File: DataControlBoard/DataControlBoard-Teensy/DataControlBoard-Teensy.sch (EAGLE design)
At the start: 1 part

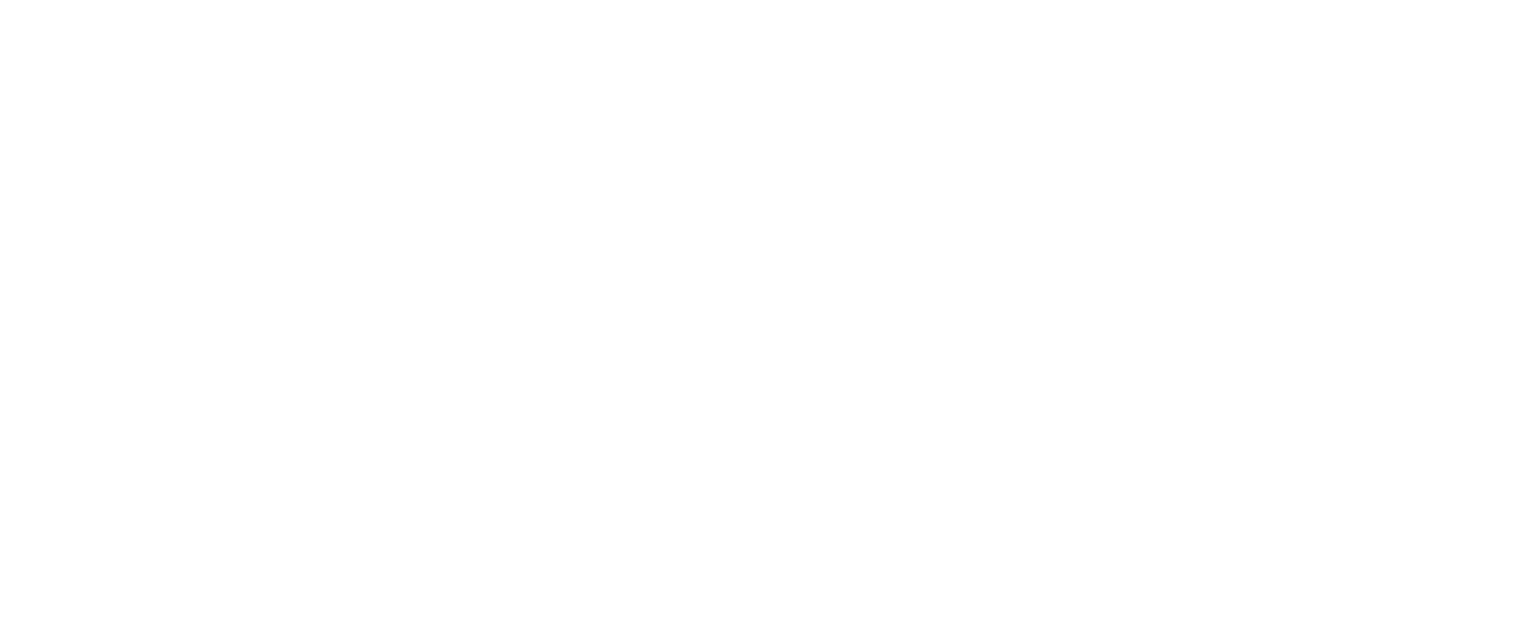
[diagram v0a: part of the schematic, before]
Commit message: Added micro-d25 connectors to lib, added to schem
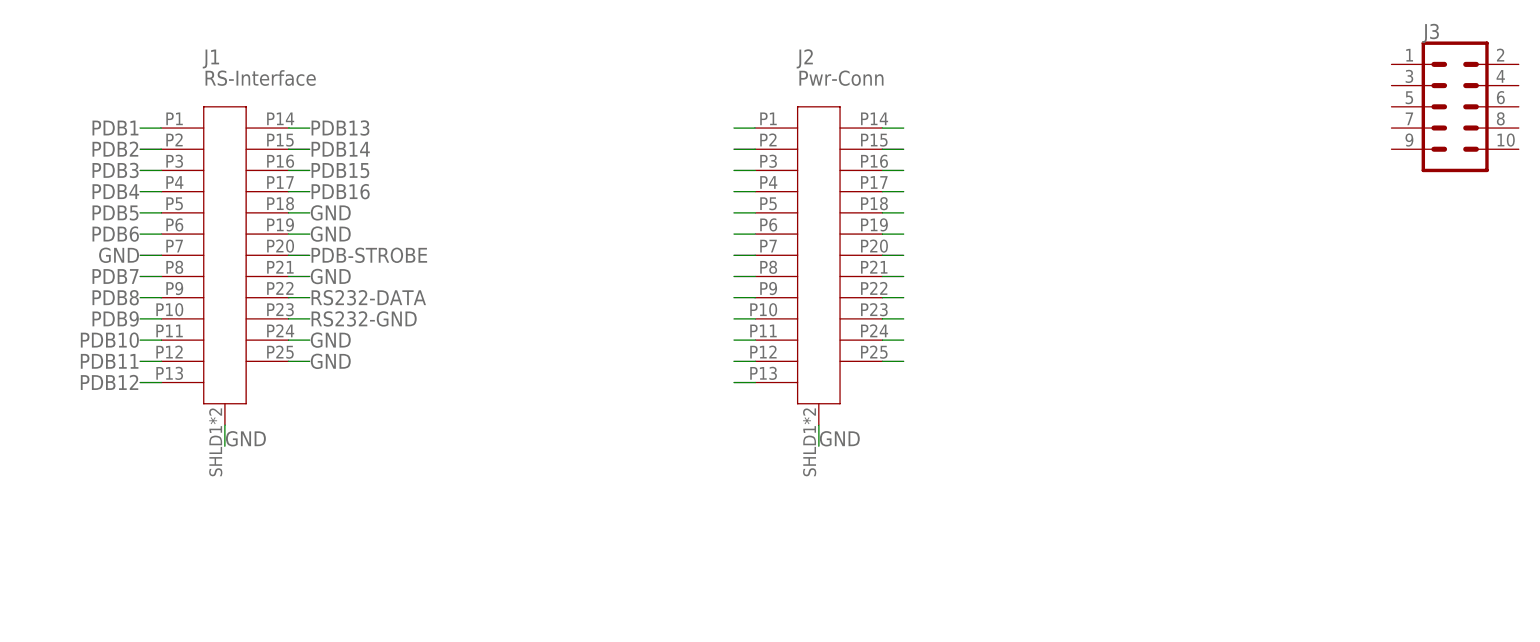
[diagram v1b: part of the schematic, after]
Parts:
- added J1: RS-Interface, RPi-Parts:MICRO-D25
- added J2: Pwr-Conn, RPi-Parts:MICRO-D25
- added J3: (no value), SparkFun-Connectors:CONN_05X2PTH
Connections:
- new net GND: J1.P18, J1.P19, J1.P21, J1.P24, J1.P25, J1.P7, J1.SHLD, J2.SHLD
- new net N$26: J2.P14
- new net N$27: J2.P15
- new net N$28: J2.P16
- new net N$29: J2.P17
- new net N$30: J2.P18
- new net N$31: J2.P19
- new net N$32: J2.P20
- new net N$33: J2.P21
- new net N$34: J2.P22
- new net N$35: J2.P23
- new net N$36: J2.P24
- new net N$37: J2.P25
- new net N$38: J2.P13
- new net N$39: J2.P12
- new net N$40: J2.P11
- new net N$41: J2.P10
- new net N$42: J2.P9
- new net N$43: J2.P8
- new net N$44: J2.P7
- new net N$45: J2.P6
- new net N$46: J2.P5
- new net N$47: J2.P4
- new net N$48: J2.P3
- new net N$49: J2.P2
- new net N$50: J2.P1
- new net PDB-STROBE: J1.P20
- new net PDB1: J1.P1
- new net PDB10: J1.P11
- new net PDB11: J1.P12
- new net PDB12: J1.P13
- new net PDB13: J1.P14
- new net PDB14: J1.P15
- new net PDB15: J1.P16
- new net PDB16: J1.P17
- new net PDB2: J1.P2
- new net PDB3: J1.P3
- new net PDB4: J1.P4
- new net PDB5: J1.P5
- new net PDB6: J1.P6
- new net PDB7: J1.P8
- new net PDB8: J1.P9
- new net PDB9: J1.P10
- new net RS232-DATA: J1.P22
- new net RS232-GND: J1.P23

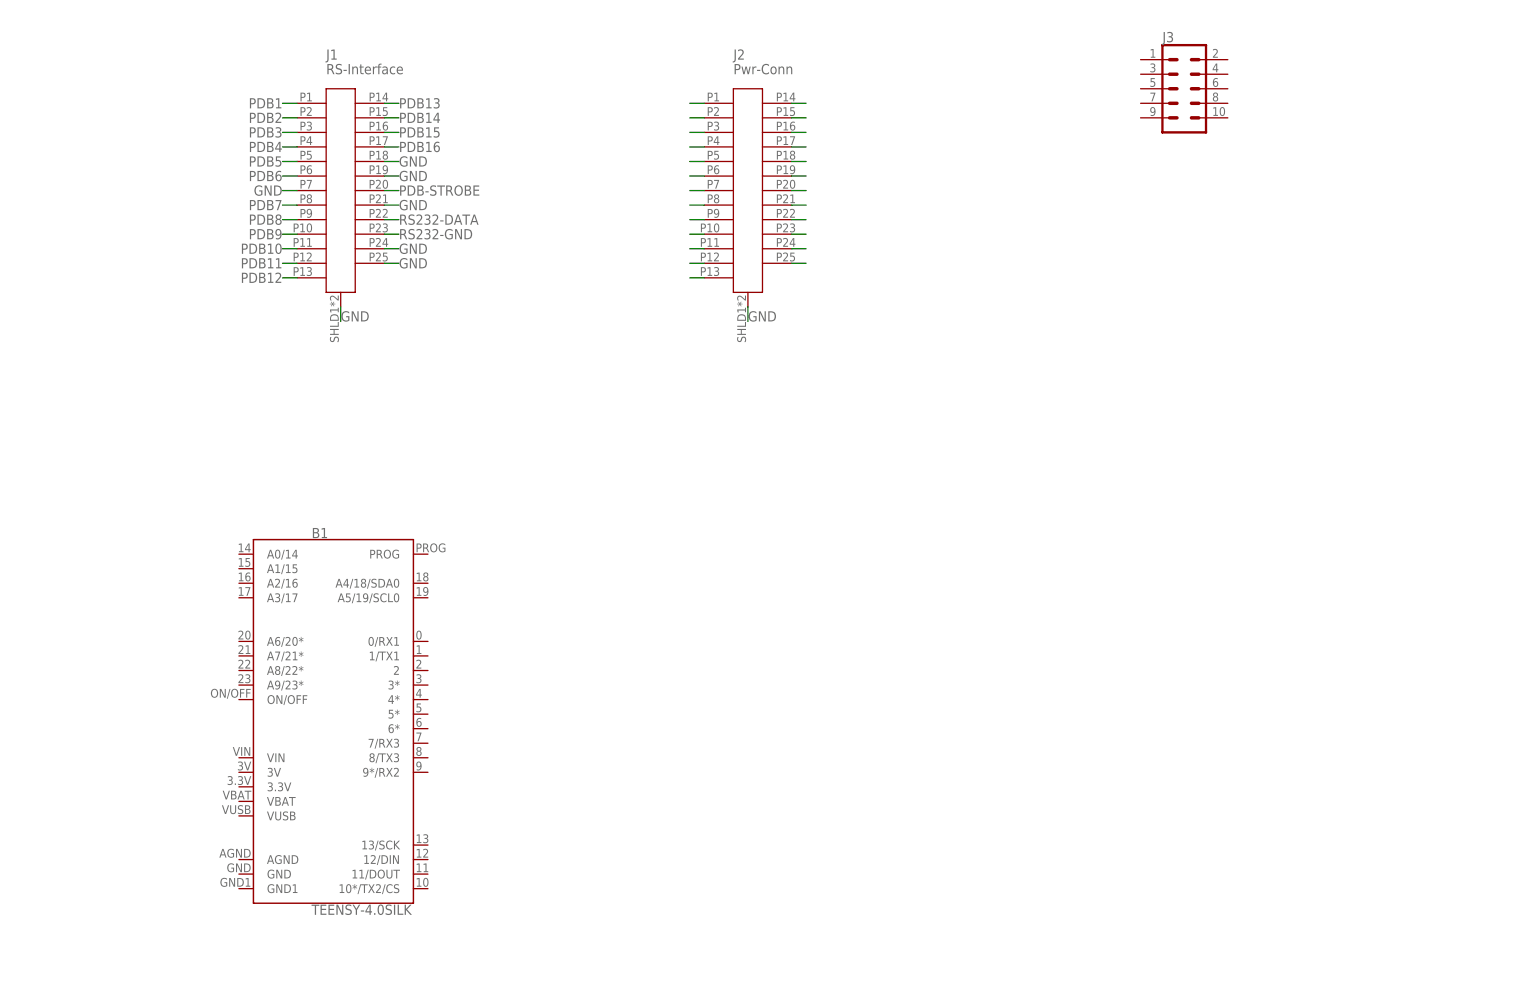
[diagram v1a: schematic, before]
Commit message: Added some parts and routes. Exposed bottom of teensy
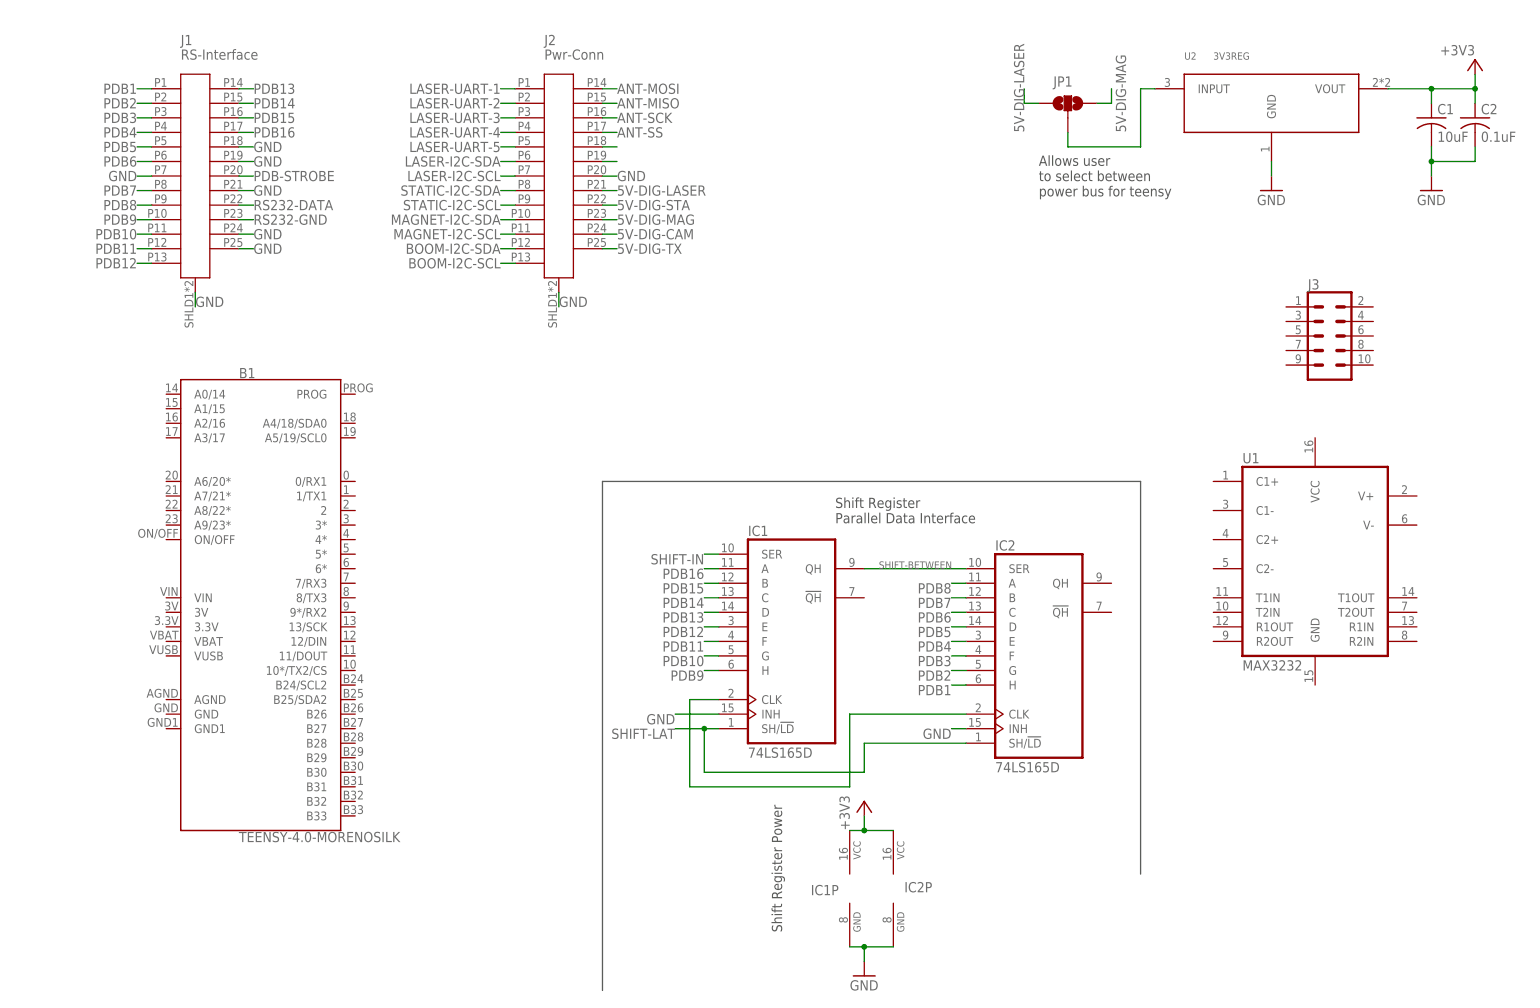
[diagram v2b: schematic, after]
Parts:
- added C1: 10uF, rcl:C-USC0805
- added C2: 0.1uF, rcl:C-USC0805
- added IC1, IC2: 74LS165D, 74xx-us:74LS165D
- added JP1: JUMPER-SMT_3_NO_NO-SILK, SparkFun-Jumpers:JUMPER-SMT_3_NO_NO-SILK
- added U1: MAX3232, SparkFun-IC-Comms:MAX2323SOIC16
- added U2: 3V3REG, PowerManagementParts:3V3REG
- B1: value TEENSY-4.0SILK -> TEENSY-4.0-MORENOSILK; device PowerManagementParts:TEENSY-4.0SILK -> RPi-Parts:TEENSY-4.0-MORENOSILK
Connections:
- net N$26 renamed ANT-MOSI
- net N$27 renamed ANT-MISO
- net N$28 renamed ANT-SCK
- net N$29 renamed ANT-SS
- net N$34 renamed 5V-DIG-STA
- net N$36 renamed 5V-DIG-CAM
- net N$37 renamed 5V-DIG-TX
- net N$38 renamed BOOM-I2C-SCL
- net N$39 renamed BOOM-I2C-SDA
- net N$40 renamed MAGNET-I2C-SCL
- net N$41 renamed MAGNET-I2C-SDA
- net N$42 renamed STATIC-I2C-SCL
- net N$43 renamed STATIC-I2C-SDA
- net N$44 renamed LASER-I2C-SCL
- net N$45 renamed LASER-I2C-SDA
- net N$46 renamed LASER-UART-5
- net N$47 renamed LASER-UART-4
- net N$48 renamed LASER-UART-3
- net N$49 renamed LASER-UART-2
- net N$50 renamed LASER-UART-1
- removed net N$32: J2.P20
- removed net N$33: J2.P21
- removed net N$35: J2.P23
- new net +3V3: C1.1, C2.1, IC1P.VCC, IC2P.VCC, U2.VOUT
- new net 5V-DIG-LASER: J2.P21, JP1.1
- new net 5V-DIG-MAG: J2.P23, JP1.3
- new net N$1: IC1A.CLK, IC2A.CLK
- new net N$4: JP1.2, U2.INPUT
- new net SHIFT-BETWEEN: IC1A.QH, IC2A.SER
- new net SHIFT-IN: IC1A.SER
- new net SHIFT-LAT: IC1A.SH/!LD, IC2A.SH/!LD
- net GND: now also C1.2, C2.2, IC1A.INH, IC1P.GND, IC2A.INH, IC2P.GND, J2.P20, U2.GND
- net PDB1: now also IC2A.H
- net PDB10: now also IC1A.G
- net PDB11: now also IC1A.F
- net PDB12: now also IC1A.E
- net PDB13: now also IC1A.D
- net PDB14: now also IC1A.C
- net PDB15: now also IC1A.B
- net PDB16: now also IC1A.A
- net PDB2: now also IC2A.G
- net PDB3: now also IC2A.F
- net PDB4: now also IC2A.E
- net PDB5: now also IC2A.D
- net PDB6: now also IC2A.C
- net PDB7: now also IC2A.B
- net PDB8: now also IC2A.A
- net PDB9: now also IC1A.H
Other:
- note added: "Allows user to select between power bus for teensy"
- note added: "Shift Register Parallel Data Interface"
- note added: "Shift Register Power"
- moved on the sheet: J1, J2, J3

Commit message: Schematic mostly done. Needs rpi backplane mating header, and a bunch of jumpers
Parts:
- added J4: Magnet RPi, SparkFun-Connectors:CONN_05X2PTH
- added J5: Laser RPi, SparkFun-Connectors:CONN_05X2PTH
- added JP2, JP3: JUMPER-SMT_3_NO_NO-SILK, SparkFun-Jumpers:JUMPER-SMT_3_NO_NO-SILK
- added R1, R2, R3, R4, R5, R6: 4.7k, rcl:R-US_R0805
- added R7: 10k, rcl:R-US_R0805
- added R8: 15k, rcl:R-US_R0805
- J3: value (none) -> Static RPi
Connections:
- net N$4 renamed +5V
- new net LAS-COMM-EN: B1.B32, J5.9
- new net MAG-COMM-EN: B1.B31, J4.9
- new net N$10: J5.8
- new net N$11: J5.10
- new net N$12: B1.3*
- new net N$13: J4.2
- new net N$14: J4.4
- new net N$15: J4.6
- new net N$16: J4.8
- new net N$17: J4.10
- new net N$18: J3.5
- new net N$19: J3.7
- new net N$2: J4.5
- new net N$20: B1.4*
- new net N$21: J3.2
- new net N$22: J3.4
- new net N$23: J3.6
- new net N$24: J3.8
- new net N$25: J3.10
- new net N$26: B1.5*
- new net N$3: J4.7
- new net N$4: J5.5
- new net N$5: J5.7
- new net N$7: J5.2
- new net N$8: J5.4
- new net N$9: J5.6
- new net PDB-STROBE-3V3: B1.2, R7.1, R8.2
- new net PI-SCL: B1.B24/SCL2, J3.3, J4.3, J5.3, R2.1
- new net PI-SDA: B1.B25/SDA2, J3.1, J4.1, J5.1, R1.1
- new net SCL0: B1.A5/19/SCL0, R4.1
- new net SCL1: B1.A2/16, R6.1
- new net SDA0: B1.A4/18/SDA0, R3.1
- new net SDA1: B1.A3/17, R5.1
- new net STA-COMM-EN: B1.B30, J3.9
- new net UART-TX: B1.8/TX3
- net +3V3: now also B1.3.3V, R1.2, R2.2, R3.2, R4.2, R5.2, R6.2
- net GND: now also B1.AGND, B1.GND, B1.GND1, R8.1
- net PDB-STROBE: now also R7.2
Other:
- note added: "5V GND GPIO14 GPIO15 GPIO18"
- note added: "GPIO from Pi:"
- note added: "Level Shift from 5V to 3.3V"
- note added: "SDA SCL GPIO4 GND GPIO17"
